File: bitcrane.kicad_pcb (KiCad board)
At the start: 4 copper layers, 110 x 100 mm, 123 parts, among them J1 0455580003, J10 PSU Comm, J11 0353180420, J12 0353180420, J13 0353180420, J14 0353180420, J15 Conn_01x04, J2 USB_C_Receptacle_USB2.0, J3 2x9P 2mm, J4 2x9P 2mm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

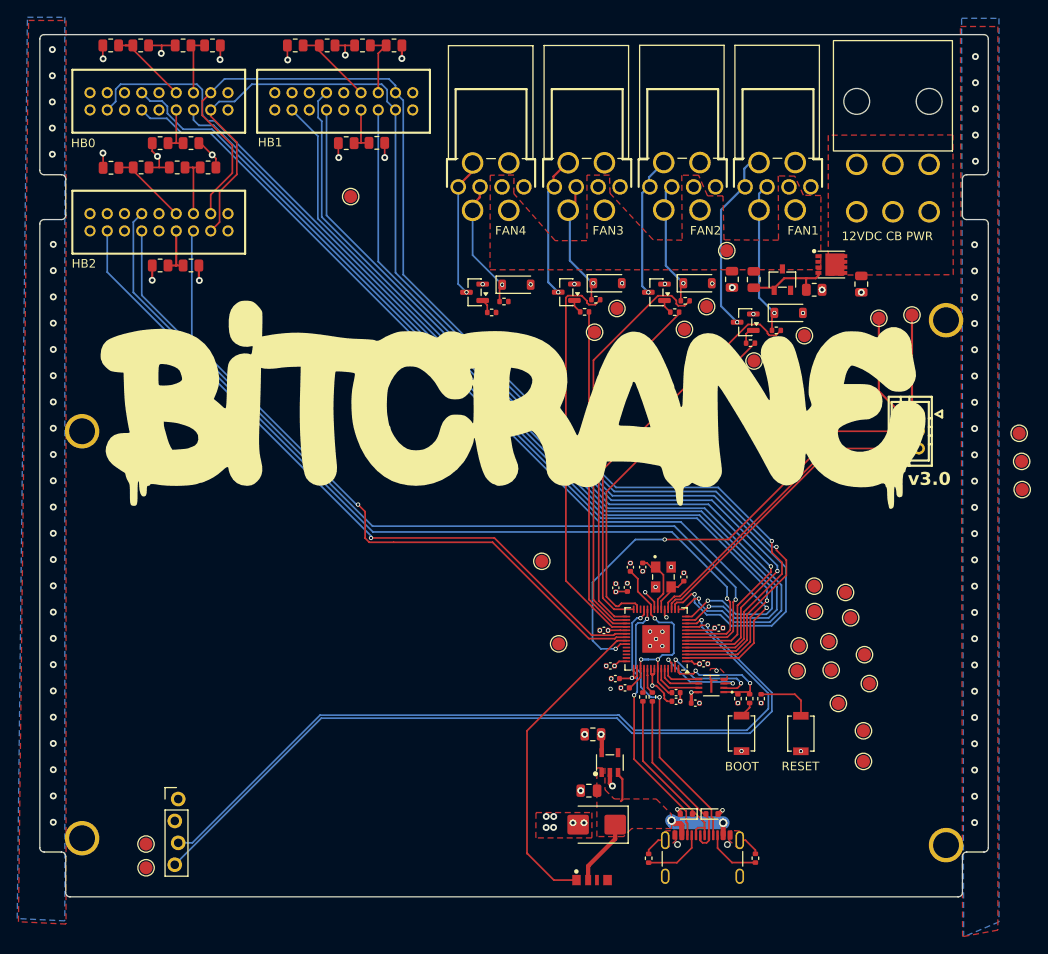
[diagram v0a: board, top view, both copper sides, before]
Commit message: switch to bigger 3.3V LDO. add 3D parts
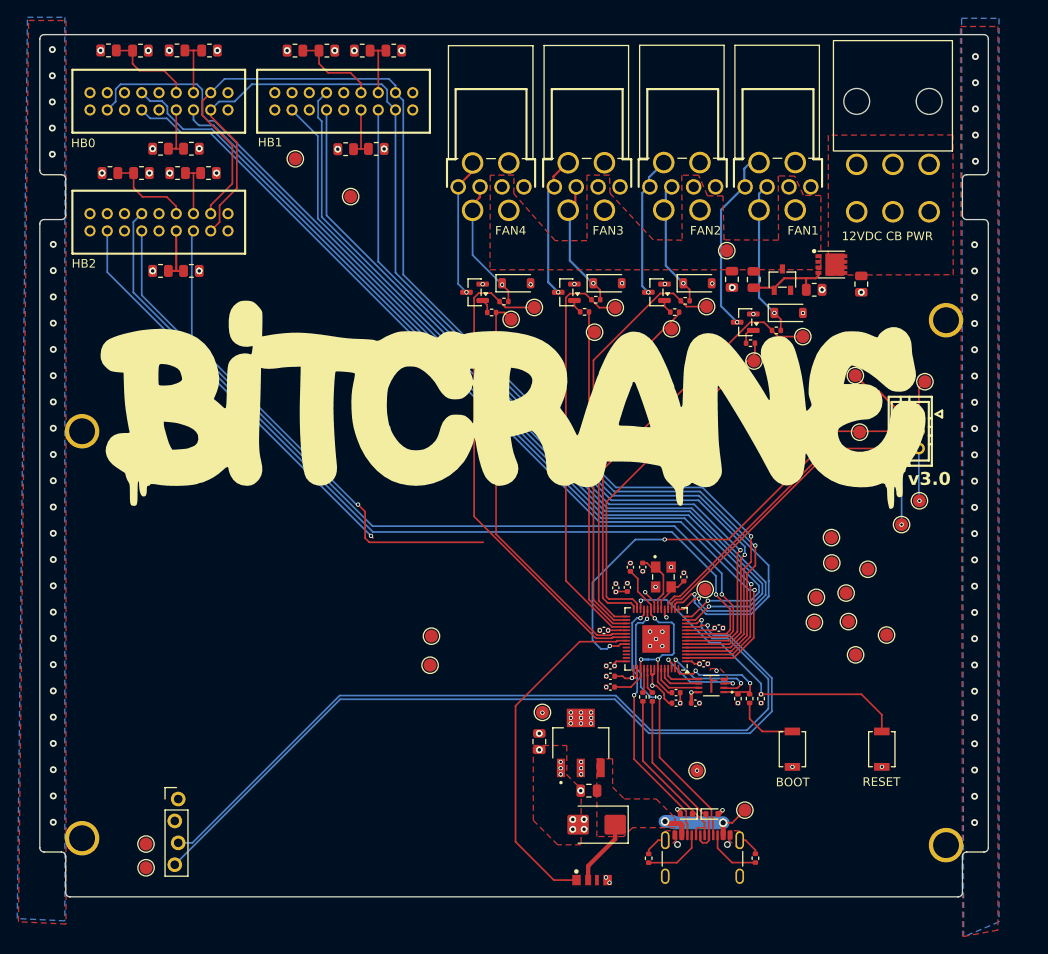
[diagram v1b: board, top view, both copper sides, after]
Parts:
- added TP31: TestPoint, TestPoint:TestPoint_Pad_D1.5mm, F.Cu at (134.5, 119.6)
- added TP32: TestPoint, TestPoint:TestPoint_Pad_D1.5mm, F.Cu at (112.9, 67.3)
- added TP33: TestPoint, TestPoint:TestPoint_Pad_D1.5mm, F.Cu at (115.6, 65.9)
- U4: value RT9080-33GJ5 -> TLV1117LV33DCYR; footprint bitcrane:TSOT-23-5_L2.9-W1.6-P0.95-LS2.8-BL -> bitcrane:VREG_TLV1117LV33DCYR
- moved TP17 81.2 mm to (87.9, 48.6)
- moved TP2 37.7 mm to (116.5, 112.8)
- moved TP4 20.0 mm to (153.3, 80.3)
- moved TP16 20.0 mm to (135.4, 98.6)
- moved TP1 16.5 mm to (140.0, 124.2)
- moved TP20 15.7 mm to (158.2, 91.1)
- moved TP27 15.5 mm to (103.7, 104.0)
- moved TP28 15.1 mm to (103.5, 107.4)
- moved TP19 14.0 mm to (160.3, 88.3)
- moved SW1 9.56 mm to (155.9, 117.1)
- moved TP29 7.88 mm to (160.9, 74.5)
- moved TP30 7.19 mm to (152.8, 73.8)
- moved C3 6.27 mm to (116.2, 116.2), turned to -90 degrees
- moved SW2 6.18 mm to (145.5, 117.1)
- moved TP11 5.97 mm to (156.5, 103.9)
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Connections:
- U4 pad 1: /5V -> GND
- U4 pad 2: GND -> /3V3
- U4 pad 4: unconnected-(U4-NC-Pad4) -> /3V3
- U6 pad 34: /RST2 -> /FAN4_PWM
- U6 pad 35: /PLUG2 -> /FAN4_TACH
- U6 pad 38: unconnected-(U6-GPIO26_ADC0-Pad38) -> /RST2
- U6 pad 39: unconnected-(U6-GPIO27_ADC1-Pad39) -> /PLUG2
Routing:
- net /FAN4_TACH: track 0.00 -> 56.8 mm
- net /FAN4_PWM: track 0.00 -> 47.8 mm
- net /RST2: track 82.6 -> 48.4 mm
- net Net-(U6-RUN): track 6.61 -> 37.1 mm, vias 0 -> 2
- net /PLUG2: track 79.4 -> 58.0 mm
- net GND: track 27.4 -> 10.0 mm, vias 108 -> 114
- net /3V3: track 43.3 -> 26.6 mm, vias 20 -> 34
- net /PSU_SCL: track 35.3 -> 44.1 mm, vias 0 -> 1
- net Net-(J10-Pin_1): track 11.8 -> 4.03 mm
- net /PSU_SDA: track 36.8 -> 42.9 mm, vias 0 -> 1
- net /PLUG1: track 101.4 -> 95.4 mm
- net /RST1: track 102.6 -> 97.0 mm
- net Net-(R5-Pad2): track 1.86 -> 7.40 mm
- net /RST0: track 120.4 -> 115.1 mm
- net /PLUG0: track 104.8 -> 99.6 mm
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
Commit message: drc check. copy over missing footprints to bitcrane library
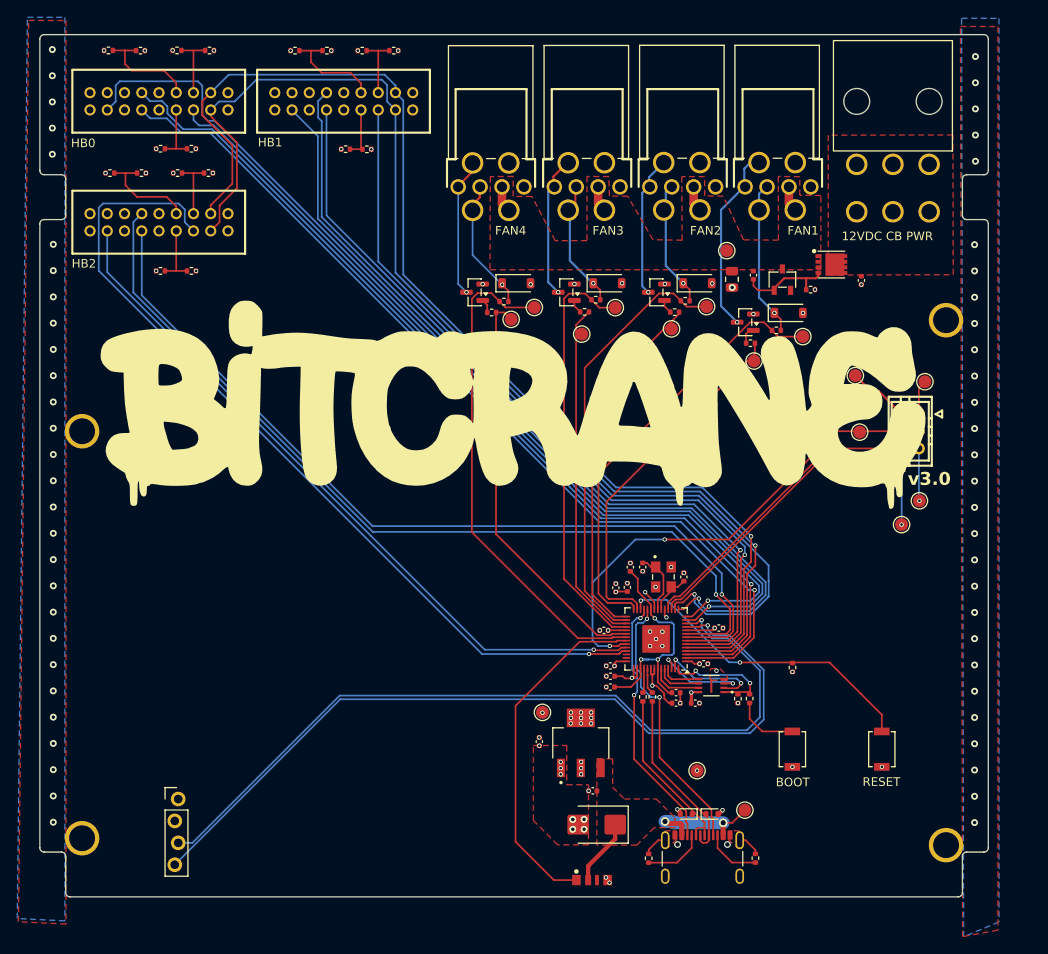
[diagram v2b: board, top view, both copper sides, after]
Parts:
- removed TP10, TP11, TP12, TP13, TP14, TP15, TP16, TP17, TP18, TP27, TP28, TP5, TP6, TP7, TP8, TP9: TestPoint, TestPoint:TestPoint_Pad_D1.5mm
- C1, C2, C3, C4: footprint Capacitor_SMD:C_0805_2012Metric -> Capacitor_SMD:C_0402_1005Metric
- J2: footprint aditBoard:USB_C_Receptacle_GCT_USB4105-xx-A_16P_TopMnt_Horizontal -> bitcrane:USB_C_Receptacle_GCT_USB4105-xx-A_16P_TopMnt_Horizontal
- R17, R18, R19, R20, R21, R22, R23, R24, R25, R26, R27, R28, R29, R3, R30, R31, R32, R33, R34: footprint Resistor_SMD:R_0805_2012Metric -> Resistor_SMD:R_0402_1005Metric
- U3: footprint emberone:USON-8_UX_2x3x0p6_WIN -> bitcrane:USON-8_UX_2x3x0p6_WIN
- U6: footprint Package_DFN_QFN:QFN-56-1EP_7x7mm_P0.4mm_EP3.2x3.2mm -> bitcrane:QFN-56-1EP_7x7mm_P0.4mm_EP3.2x3.2mm
- U7: footprint emberone:LED-SMD_4P-L4.0-W1.6-L -> bitcrane:LED-SMD_4P-L4.0-W1.6-L
- Y1: footprint emberone:XTAL_ECS-120-20-33-CKM-TR3 -> bitcrane:XTAL_ECS-120-20-33-CKM-TR3
- moved R6 5.13 mm to (145.6, 107.6)
- moved TP25 1.51 mm to (121.1, 69.0)
- moved R19 1.09 mm to (96.2, 47.5)
- moved C4 0.50 mm to (141.0, 62.1)
- moved C2 0.45 mm to (122.4, 122.0)
- moved C1 0.43 mm to (153.5, 62.8)
- moved R3 0.42 mm to (147.7, 63.8)
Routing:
- net /PLUG2: track 58.0 -> 100.7 mm
- net /RST2: track 48.4 -> 83.3 mm
- net /12V: track 0.00 -> 12.0 mm
- net /A00: track 10.5 -> 12.3 mm
- net /A01: track 10.3 -> 11.9 mm
- net /FAN4_TACH: track 56.8 -> 58.3 mm
- net /A02: track 10.3 -> 11.8 mm
- net /FAN3_PWM: track 38.9 -> 40.1 mm
- net Net-(D2-A): track 9.61 -> 10.7 mm
- net /XIN: track 5.39 -> 4.35 mm
- net /FAN2_TACH: track 49.5 -> 50.5 mm
- net /DISPLAY_SCL: track 94.8 -> 93.9 mm
- net /RST0: track 115.1 -> 115.9 mm
- net /A21: track 6.73 -> 7.52 mm
- net /A22: track 6.49 -> 7.28 mm
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
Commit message: add more 3D files. rotate display 180
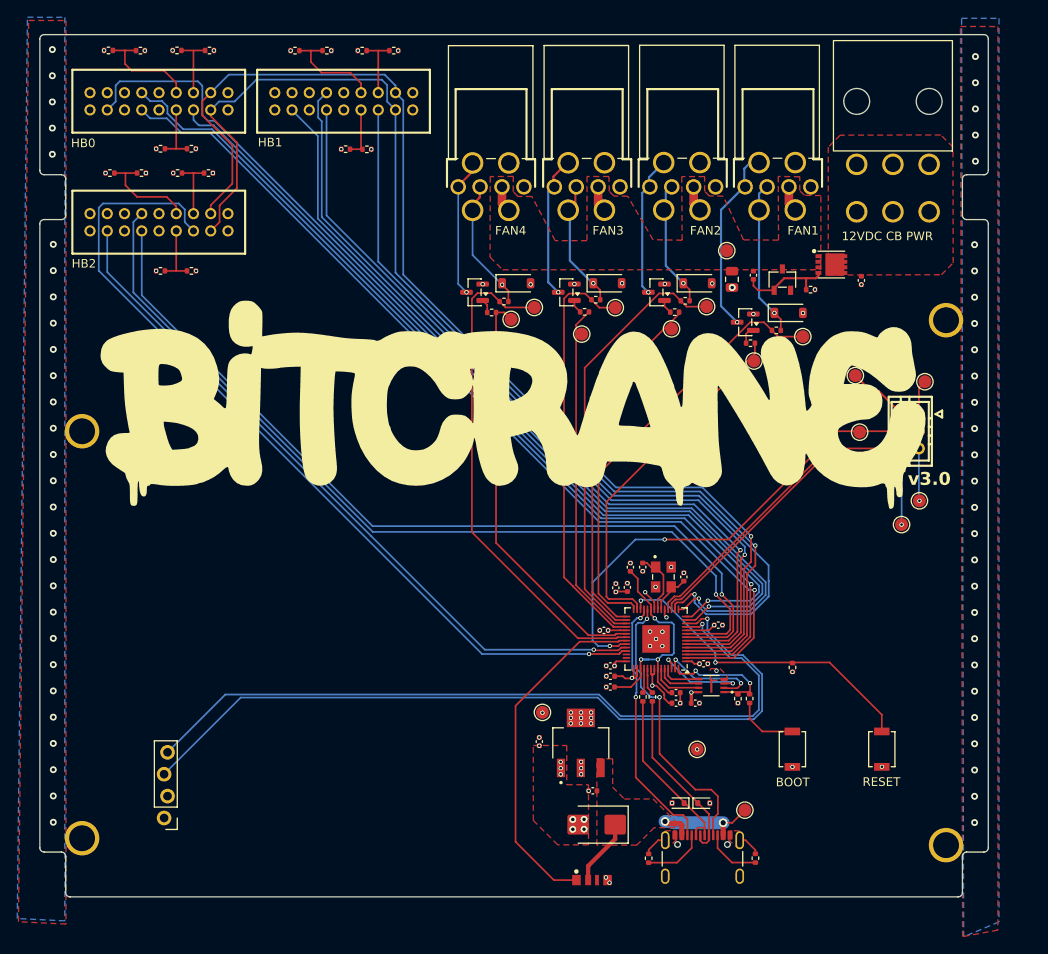
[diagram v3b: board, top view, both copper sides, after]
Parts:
- moved J15 2.53 mm to (72.9, 125.1), turned to 180 degrees
- moved TP31 2.47 mm to (134.5, 117.1)
- moved U1 1.58 mm to (135.3, 123.4)
- moved U2 1.58 mm to (132.3, 123.4)
- moved C18 0.35 mm to (136.9, 102.7)
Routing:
- net /DISPLAY_SDA: track 95.8 -> 88.2 mm
- net /DISPLAY_SCL: track 93.9 -> 91.3 mm
- net /SWCLK: track 31.3 -> 32.9 mm
- net GND: track 9.97 -> 8.83 mm
- net Net-(U6-RUN): track 36.4 -> 37.1 mm
- net /FAN4_PWM: track 47.8 -> 48.4 mm

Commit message: change buttons to LCSC versions. add preliminary LCSC part numbers for everything
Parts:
- SW1: footprint bitaxe:SW_CS1213AGF260_CRS -> bitcrane:SW-SMD_L3.9-W3.0-P4.45
- SW2: value GT-TC029B-H025-L1N -> ~; footprint bitaxe:SW_CS1213AGF260_CRS -> bitcrane:SW-SMD_L3.9-W3.0-P4.45

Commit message: removed old libraries
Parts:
- J10: footprint bitcart:CONN-TH_6P-P2.00_PHD-2X3A -> bitcrane:CONN-TH_6P-P2.00_PHD-2X3A
- J3, J4, J5: footprint bitcart:CONN-TH_X2026WV-2-09D-46SN -> bitcrane:CONN-TH_X2026WV-2-09D-46SN
- SW1: value GT-TC029B-H025-L1N -> TS-1088-AR02016
- SW2: value ~ -> TS-1088-AR02016

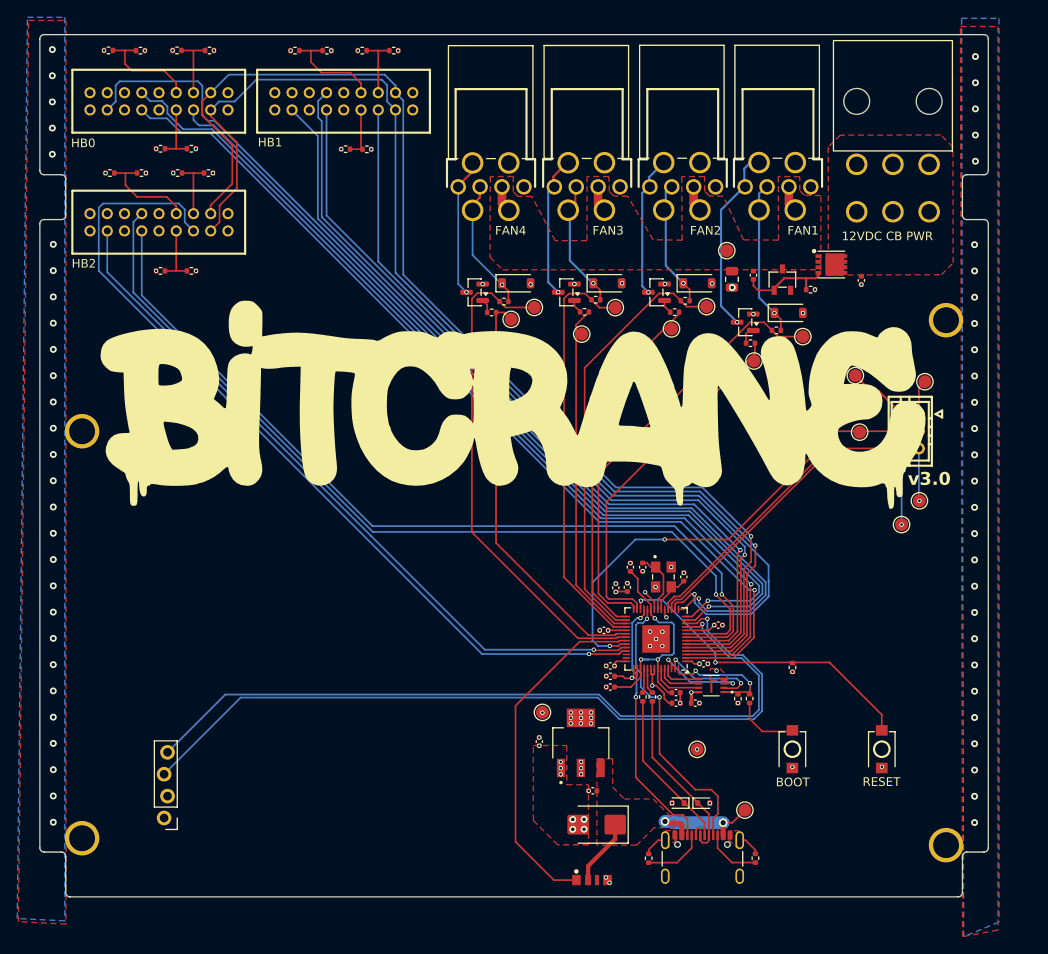
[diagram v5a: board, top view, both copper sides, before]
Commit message: update test points and cleanup silkscreen. add render to readme.
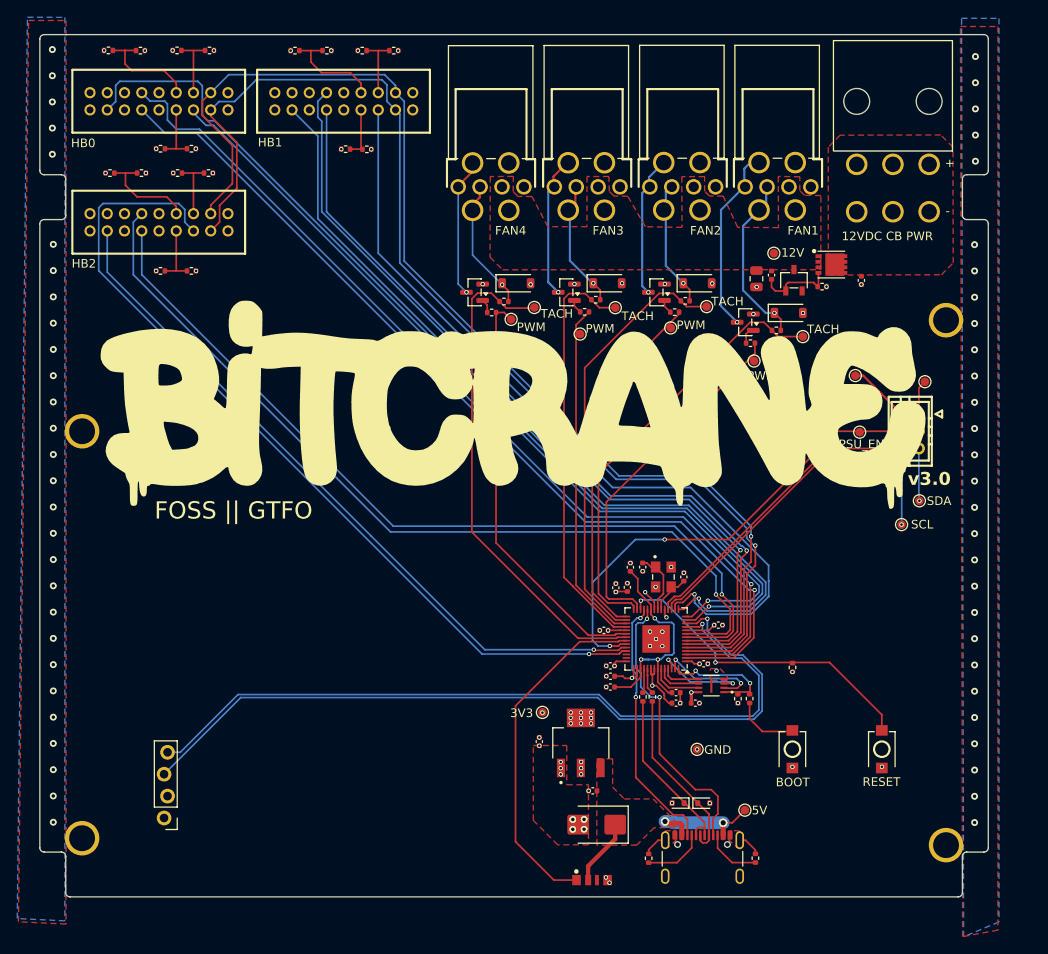
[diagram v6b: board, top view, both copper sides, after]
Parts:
- TP1: value TestPoint -> 5V; footprint TestPoint:TestPoint_Pad_D1.5mm -> bitcrane:TestPoint_Pad_D1.0mm
- TP19: value TestPoint -> SDA; footprint TestPoint:TestPoint_Pad_D1.5mm -> bitcrane:TestPoint_Pad_D1.0mm
- TP2: value TestPoint -> 3V3; footprint TestPoint:TestPoint_Pad_D1.5mm -> bitcrane:TestPoint_Pad_D1.0mm
- TP20: value TestPoint -> SCL; footprint TestPoint:TestPoint_Pad_D1.5mm -> bitcrane:TestPoint_Pad_D1.0mm
- TP21, TP23, TP25, TP32: value TestPoint -> PWM; footprint TestPoint:TestPoint_Pad_D1.5mm -> bitcrane:TestPoint_Pad_D1.0mm
- TP22, TP24, TP26, TP33: value TestPoint -> TACH; footprint TestPoint:TestPoint_Pad_D1.5mm -> bitcrane:TestPoint_Pad_D1.0mm
- TP29, TP30: footprint TestPoint:TestPoint_Pad_D1.5mm -> bitcrane:TestPoint_Pad_D1.0mm
- TP3: value TestPoint -> 12V; footprint TestPoint:TestPoint_Pad_D1.5mm -> bitcrane:TestPoint_Pad_D1.0mm
- TP31: value TestPoint -> GND; footprint TestPoint:TestPoint_Pad_D1.5mm -> bitcrane:TestPoint_Pad_D1.0mm
- TP4: value TestPoint -> PSU_EN; footprint TestPoint:TestPoint_Pad_D1.5mm -> bitcrane:TestPoint_Pad_D1.0mm
- moved TP3 5.47 mm to (143.4, 59.6)
- moved C5 2.84 mm to (141.4, 62.6)
- moved C4 2.10 mm to (143.1, 62.1)
- moved R3 1.38 mm to (149.0, 63.5)
- moved D2 1.34 mm to (145.7, 62.7)
- moved TP25 0.19 mm to (120.9, 69.0)
- moved TP23 0.14 mm to (131.4, 68.3)
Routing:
- net /12V: track 12.0 -> 0.00 mm
- net /FAN1_TACH_PIN: track 19.4 -> 21.6 mm
- net Net-(D2-A): track 10.7 -> 9.10 mm
- net /TXD2: track 101.2 -> 99.8 mm
- net /RXD2: track 103.0 -> 101.8 mm
- net /RXD0: track 109.3 -> 109.9 mm
- net /PLUG1: track 95.4 -> 94.8 mm
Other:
- board text added: "+"
- board text added: "-"
- board text added: "FOSS || GTFO"
